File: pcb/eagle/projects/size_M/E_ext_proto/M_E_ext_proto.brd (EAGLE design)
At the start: 12 parts

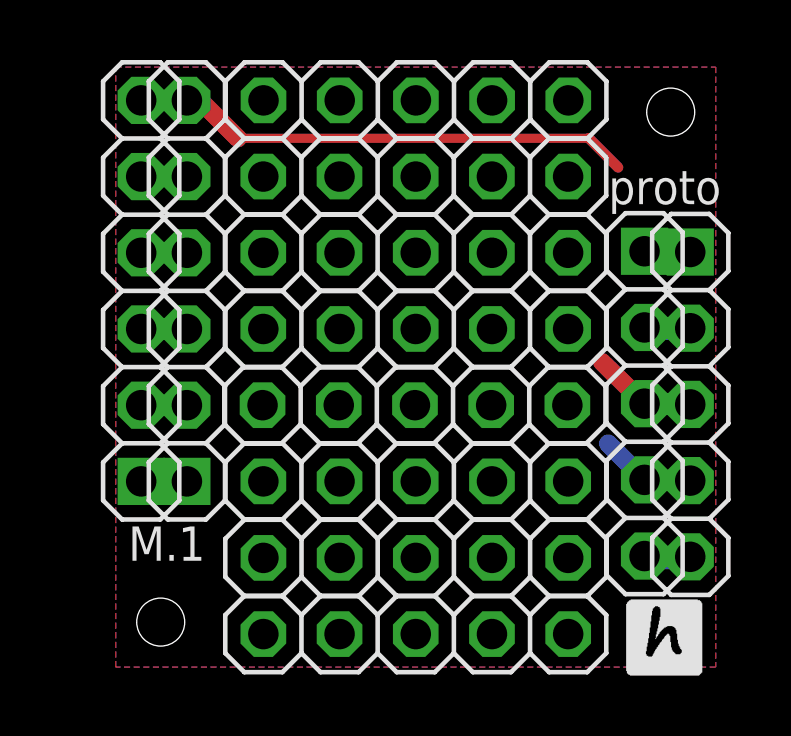
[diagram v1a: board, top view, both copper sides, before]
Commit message: PCB's adjustments + sensor extension
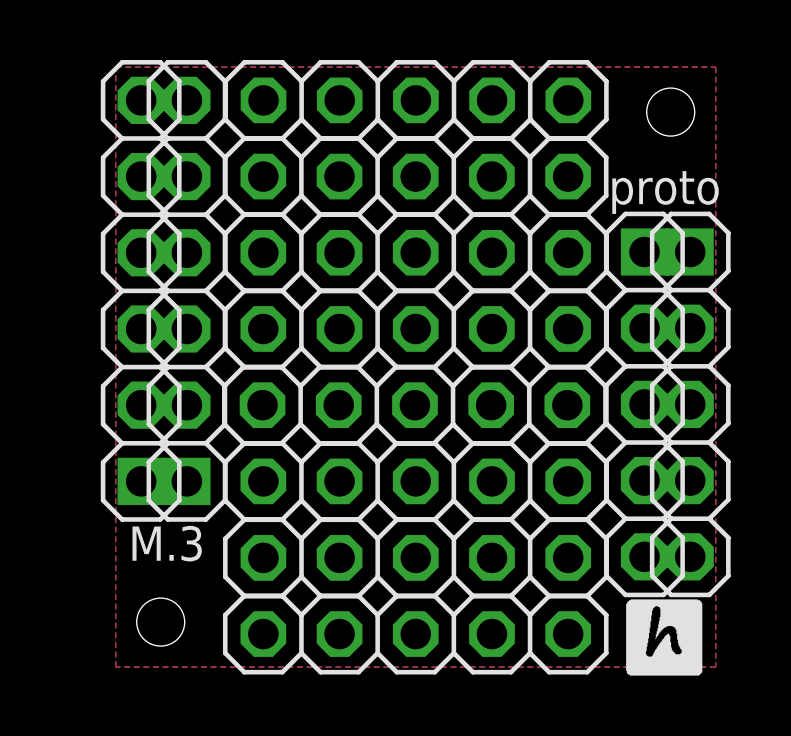
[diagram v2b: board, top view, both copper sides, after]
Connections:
- removed net VDD: JP11.4, JP3.4
- new net N$10: JP11.3, JP3.3
- net GND: now also JP11.4, JP3.4; no longer JP11.3, JP3.3
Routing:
- net GND: track 22.1 -> 0.00 mm
- net VDD: track 3.36 -> 0.00 mm
- net N$10: track 0.00 -> 1.54 mm
- added copper zone on layer 16, net GND
- removed copper zone on layer 16, net VDD
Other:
- board text added: "M.3"
- board text removed: "M.1"
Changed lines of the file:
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@@
 <setting verticaltext="up"/>
 </settings>
-<grid distance="1" unitdist="mm" unit="mm" style="lines" multiple="1" display="yes" altdistance="0.1" altunitdist="mm" altunit="mm"/>
+<grid distance="1" unitdist="mil" unit="mil" style="lines" multiple="1" display="yes" altdistance="0.1" altunitdist="mm" altunit="mm"/>
 <layers>
 <layer number="1" name="Top" color="4" fill="1" visible="yes" active="yes"/>
@@
 <hole x="2" y="2" drill="1.6"/>
 <circle x="2" y="2" radius="1.9" width="0.1" layer="52"/>
-<text x="3.484" y="5.1866" size="1.143" layer="21" rot="R180">M.1</text>
+<text x="3.484" y="5.1866" size="1.143" layer="21" rot="R180">M.3</text>
 <text x="20.6798" y="17.0738" size="1.143" layer="21" rot="R180">proto</text>
 <rectangle x1="17.6403" y1="0.2159" x2="19.9517" y2="0.2413" layer="21"/>
@@
 <attribute name="VALUE" x="6.048" y="5.42" size="1.27" layer="27" rot="R90"/>
 </element>
-<element name="JP3" library="pinhead2" package="1X05" package3d_urn="urn:adsk.eagle:package:22469/2" value="" x="18.127" y="9.2808" smashed="yes" rot="R270">
-<attribute name="POPULARITY" value="69" x="18.127" y="9.2808" size="1.778" layer="27" rot="R270" display="off"/>
-<attribute name="VALUE" x="14.952" y="15.6308" size="1.27" layer="27" rot="R270"/>
+<element name="JP3" library="pinhead2" package="1X05" package3d_urn="urn:adsk.eagle:package:22469/2" value="" x="18.127" y="9.2554" smashed="yes" rot="R270">
+<attribute name="POPULARITY" value="69" x="18.127" y="9.2554" size="1.778" layer="27" rot="R270" display="off"/>
+<attribute name="VALUE" x="14.952" y="15.6054" size="1.27" layer="27" rot="R270"/>
 </element>
 </elements>
@@
 <vertex x="0.5" y="0.5"/>
 </polygon>
-<contactref element="JP11" pad="3"/>
-<wire x1="19.6508" y1="9.2554" x2="19.636590625" y2="9.241190625" width="0.3556" layer="1"/>
-<wire x1="19.636590625" y1="9.241190625" x2="18.01078125" y2="9.2" width="0.3556" layer="1"/>
-<wire x1="4.5716" y1="18.1284" x2="16.27085625" y2="18.1284" width="0.3048" layer="1"/>
-<wire x1="16.27085625" y1="18.1284" x2="17.2442" y2="17.15505625" width="0.3556" layer="1"/>
-<contactref element="JP3" pad="3"/>
-<wire x1="19.6508" y1="9.2554" x2="19.64805625" y2="9.151484375" width="0.6096" layer="16"/>
-<wire x1="19.64805625" y1="9.151484375" x2="19.593078125" y2="9.1946" width="0.6096" layer="16"/>
-<wire x1="19.593078125" y1="9.1946" x2="18.177534375" y2="9.230265625" width="0.6096" layer="16"/>
-<wire x1="18.127" y1="9.2808" x2="18.177534375" y2="9.230265625" width="0.6096" layer="16"/>
 <contactref element="JP2" pad="6"/>
 <contactref element="JP1" pad="6"/>
-<wire x1="2.873" y1="19.39" x2="1.670565625" y2="19.39" width="0.6096" layer="16"/>
-<wire x1="1.670565625" y1="19.39" x2="1.35811875" y2="19.377828125" width="0.6096" layer="16"/>
-<wire x1="1.35811875" y1="19.377828125" x2="1.3492" y2="19.39" width="0.6096" layer="16"/>
-<wire x1="18.127" y1="9.2808" x2="16.7132" y2="10.66515625" width="0.6096" layer="1"/>
-<wire x1="2.873" y1="19.39" x2="3.395428125" y2="19.304571875" width="0.6096" layer="1"/>
-<wire x1="3.395428125" y1="19.304571875" x2="4.5716" y2="18.1284" width="0.6096" layer="1"/>
-</signal>
-<signal name="VDD">
+<contactref element="JP11" pad="4"/>
+<contactref element="JP3" pad="4"/>
 <polygon width="0.3048" layer="16" isolate="0.3048">
 <vertex x="0.5" y="20.5"/>
@@
 <vertex x="0.5" y="0.5"/>
 </polygon>
-<contactref element="JP11" pad="4"/>
-<contactref element="JP3" pad="4"/>
-<wire x1="19.6508" y1="6.7154" x2="19.565046875" y2="6.678484375" width="0.6096" layer="16"/>
-<wire x1="19.565046875" y1="6.678484375" x2="19.544784375" y2="6.68" width="0.6096" layer="16"/>
-<wire x1="19.6508" y1="6.7154" x2="19.6254" y2="6.7408" width="0.6096" layer="16"/>
-<wire x1="19.6254" y1="6.7408" x2="18.127" y2="6.7408" width="0.6096" layer="16"/>
-<wire x1="18.127" y1="6.7408" x2="16.916646875" y2="7.95" width="0.6096" layer="16"/>
 </signal>
 <signal name="N$1">
@@
 <contactref element="JP3" pad="5"/>
 <contactref element="JP11" pad="5"/>
-<wire x1="19.6508" y1="4.1754" x2="19.6039125" y2="4.07521875" width="0.6096" layer="16"/>
-<wire x1="18.127" y1="4.2008" x2="18.205640625" y2="4.060559375" width="0.6096" layer="16"/>
-<wire x1="19.6039125" y1="4.07521875" x2="18.205640625" y2="4.060559375" width="0.6096" layer="16"/>
+<wire x1="19.6508" y1="4.1754" x2="19.64438125" y2="4.16168125" width="0.6096" layer="16"/>
+<wire x1="18.127" y1="4.1754" x2="19.634984375" y2="4.1754" width="0.6096" layer="16"/>
+<wire x1="19.64438125" y1="4.16168125" x2="19.634984375" y2="4.1754" width="0.6096" layer="16"/>
 </signal>
 <signal name="N$7">
 <contactref element="JP11" pad="2"/>
 <contactref element="JP3" pad="2"/>
-<wire x1="19.6361125" y1="11.72069375" x2="18.17269375" y2="11.705340625" width="0.6096" layer="16"/>
-<wire x1="18.127" y1="11.8208" x2="18.17269375" y2="11.705340625" width="0.6096" layer="16"/>
-<wire x1="19.6508" y1="11.7954" x2="19.6361125" y2="11.72069375" width="0.6096" layer="16"/>
+<wire x1="19.6508" y1="11.7954" x2="19.649434375" y2="11.796765625" width="0.6096" layer="16"/>
+<wire x1="18.127" y1="11.7954" x2="18.141453125" y2="11.780946875" width="0.6096" layer="16"/>
+<wire x1="19.649434375" y1="11.796765625" x2="18.141453125" y2="11.780946875" width="0.6096" layer="16"/>
 </signal>
 <signal name="N$8">
 <contactref element="JP3" pad="1"/>
 <contactref element="JP11" pad="1"/>
-<wire x1="19.6508" y1="14.3354" x2="18.087771875" y2="14.29326875" width="0.6096" layer="16"/>
-<wire x1="18.087771875" y1="14.29326875" x2="18.017746875" y2="14.3508" width="0.6096" layer="16"/>
-<wire x1="18.017746875" y1="14.3508" x2="17.974803125" y2="14.3151875" width="0.6096" layer="16"/>
-<wire x1="17.976240625" y1="14.266328125" x2="18.127" y2="14.3608" width="0.6096" layer="16"/>
-<wire x1="17.976240625" y1="14.266328125" x2="17.974803125" y2="14.3151875" width="0.6096" layer="16"/>
+<wire x1="18.127" y1="14.3354" x2="19.6508" y2="14.3354" width="0.6096" layer="16"/>
+</signal>
+<signal name="N$10">
+<contactref element="JP11" pad="3"/>
+<contactref element="JP3" pad="3"/>
+<wire x1="19.6508" y1="9.2554" x2="19.636590625" y2="9.241190625" width="0.3556" layer="1"/>
+<wire x1="19.6508" y1="9.2554" x2="19.650859375" y2="9.2554" width="0.6096" layer="16"/>
+<wire x1="18.127" y1="9.2554" x2="19.6508" y2="9.2554" width="0.6096" layer="16"/>
 </signal>
 </signals>

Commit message: updated for PCB version 4
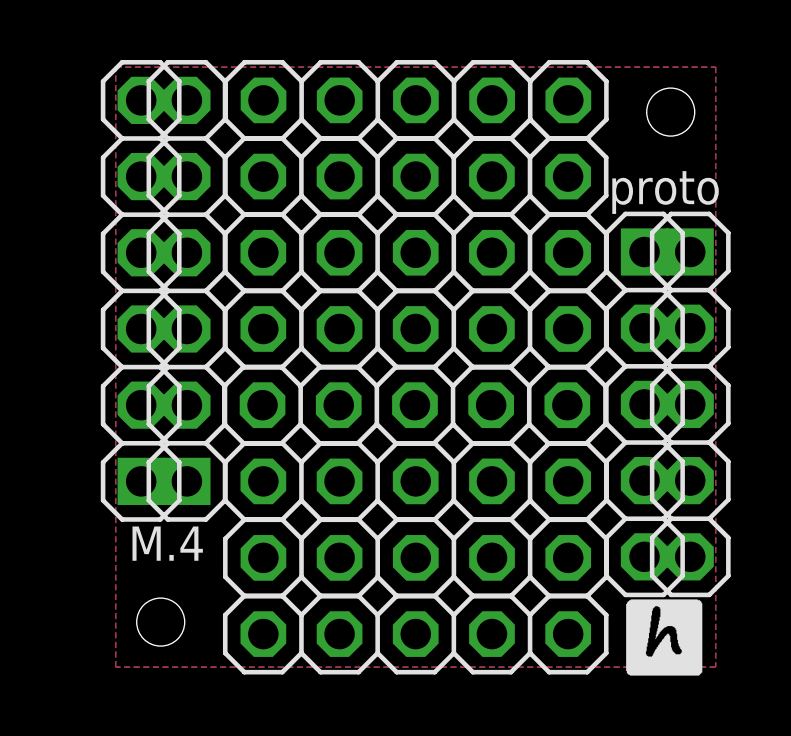
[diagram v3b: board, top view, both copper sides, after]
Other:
- board text added: "M.4"
- board text removed: "M.3"
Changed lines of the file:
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@@
 <hole x="2" y="2" drill="1.6"/>
 <circle x="2" y="2" radius="1.9" width="0.1" layer="52"/>
-<text x="3.484" y="5.1866" size="1.143" layer="21" rot="R180">M.3</text>
+<text x="3.484" y="5.1866" size="1.143" layer="21" rot="R180">M.4</text>
 <text x="20.6798" y="17.0738" size="1.143" layer="21" rot="R180">proto</text>
 <rectangle x1="17.6403" y1="0.2159" x2="19.9517" y2="0.2413" layer="21"/>

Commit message: reorganized pcb folders
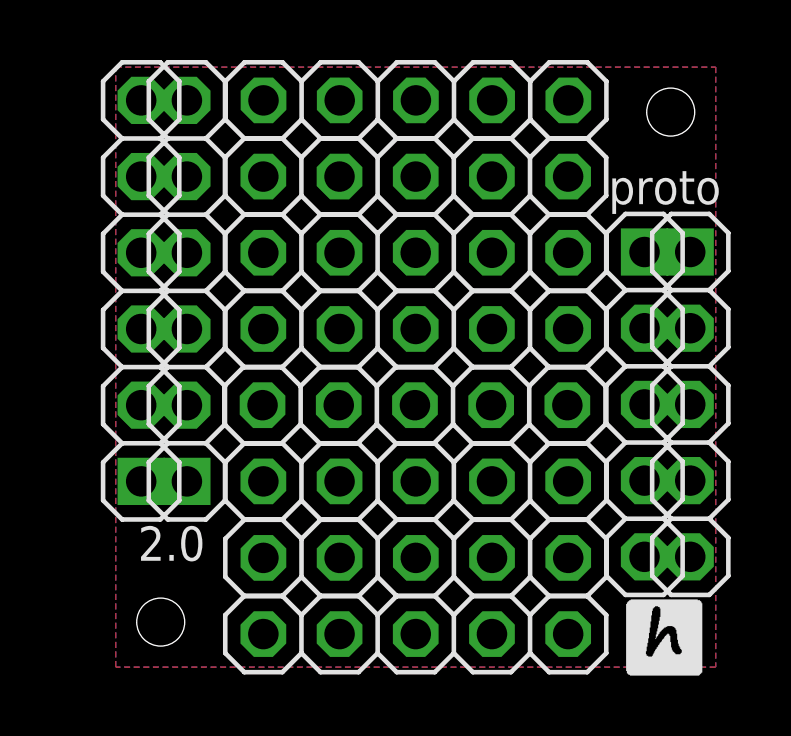
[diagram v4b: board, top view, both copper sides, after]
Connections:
- new net N$9: JP1.6, JP2.6
- net GND: no longer JP1.6, JP2.6
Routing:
- net N$9: track 0.00 -> 1.52 mm
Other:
- board text added: "2.0"
- board text removed: "M.4"
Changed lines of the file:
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@@
 <hole x="2" y="2" drill="1.6"/>
 <circle x="2" y="2" radius="1.9" width="0.1" layer="52"/>
-<text x="3.484" y="5.1866" size="1.143" layer="21" rot="R180">M.4</text>
+<text x="3.484" y="5.1866" size="1.143" layer="21" rot="R180">2.0</text>
 <text x="20.6798" y="17.0738" size="1.143" layer="21" rot="R180">proto</text>
 <rectangle x1="17.6403" y1="0.2159" x2="19.9517" y2="0.2413" layer="21"/>
@@
 <vertex x="0.5" y="0.5"/>
 </polygon>
-<contactref element="JP2" pad="6"/>
-<contactref element="JP1" pad="6"/>
 <contactref element="JP11" pad="4"/>
 <contactref element="JP3" pad="4"/>
@@
 <wire x1="18.127" y1="9.2554" x2="19.6508" y2="9.2554" width="0.6096" layer="16"/>
 </signal>
+<signal name="N$9">
+<contactref element="JP2" pad="6"/>
+<contactref element="JP1" pad="6"/>
+<wire x1="1.3492" y1="19.39" x2="2.873" y2="19.39" width="0.508" layer="16"/>
+</signal>
 </signals>

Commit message: PCB v7 * 14 pin attiny is main adapter chip now. * changed adapter pin meaning (a1-a5, swapped RX-TX, VUSB replaced by A5, top most pin changed from GND to A4) * changed usb chip of main board
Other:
- board text added: "M7"
- board text removed: "2.0"
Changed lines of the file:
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@@
 <setting verticaltext="up"/>
 </settings>
-<grid distance="1" unitdist="mil" unit="mil" style="lines" multiple="1" display="yes" altdistance="0.1" altunitdist="mm" altunit="mm"/>
+<grid distance="1" unitdist="mil" unit="mm" style="lines" multiple="1" display="yes" altdistance="0.1" altunitdist="mm" altunit="mm"/>
 <layers>
 <layer number="1" name="Top" color="4" fill="1" visible="yes" active="yes"/>
@@
 <hole x="2" y="2" drill="1.6"/>
 <circle x="2" y="2" radius="1.9" width="0.1" layer="52"/>
-<text x="3.484" y="5.1866" size="1.143" layer="21" rot="R180">2.0</text>
+<text x="3.484" y="5.1866" size="1.143" layer="21" rot="R180">M7</text>
 <text x="20.6798" y="17.0738" size="1.143" layer="21" rot="R180">proto</text>
 <rectangle x1="17.6403" y1="0.2159" x2="19.9517" y2="0.2413" layer="21"/>
@@
 <signals>
 <signal name="GND">
-<polygon width="0.3048" layer="1" isolate="0.3048">
+<polygon width="0.254" layer="1" isolate="0.254">
 <vertex x="0.5" y="20.5"/>
 <vertex x="20.5" y="20.5"/>
@@
 <contactref element="JP11" pad="4"/>
 <contactref element="JP3" pad="4"/>
-<polygon width="0.3048" layer="16" isolate="0.3048">
+<polygon width="0.254" layer="16" isolate="0.254">
 <vertex x="0.5" y="20.5"/>
 <vertex x="20.5" y="20.5"/>
